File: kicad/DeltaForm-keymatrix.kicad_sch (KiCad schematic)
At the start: 45 parts

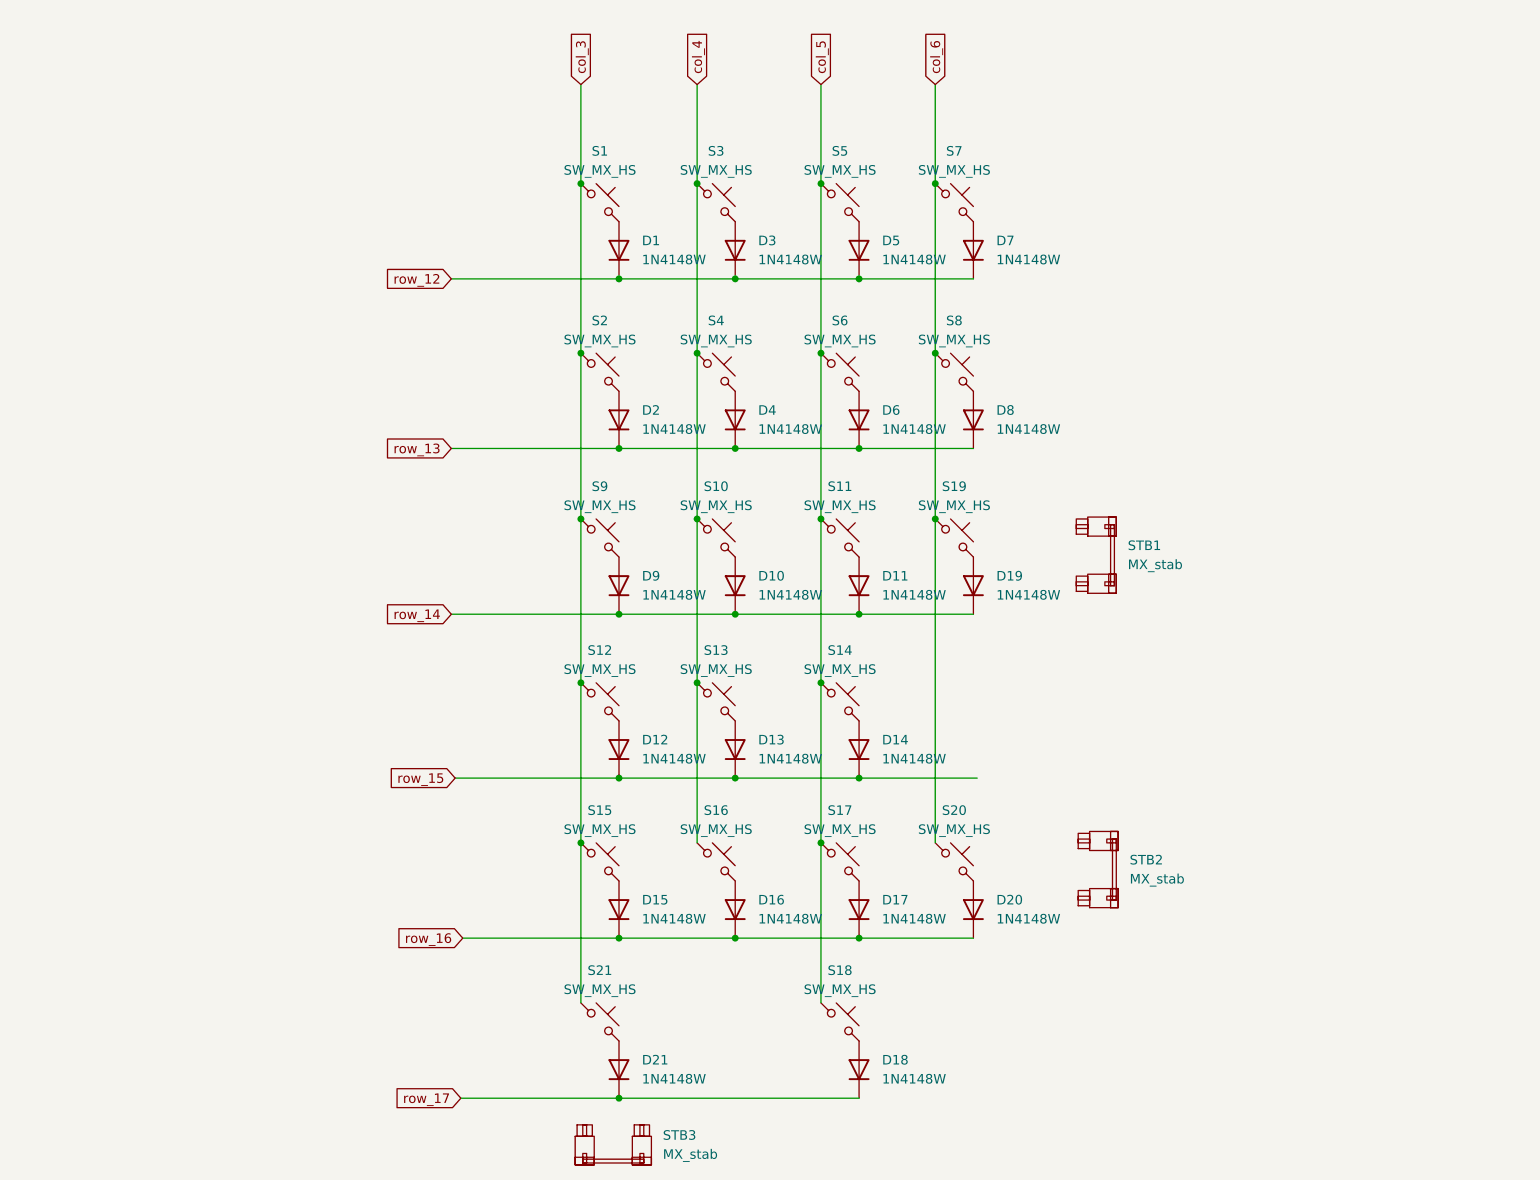
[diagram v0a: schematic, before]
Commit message: added MCU
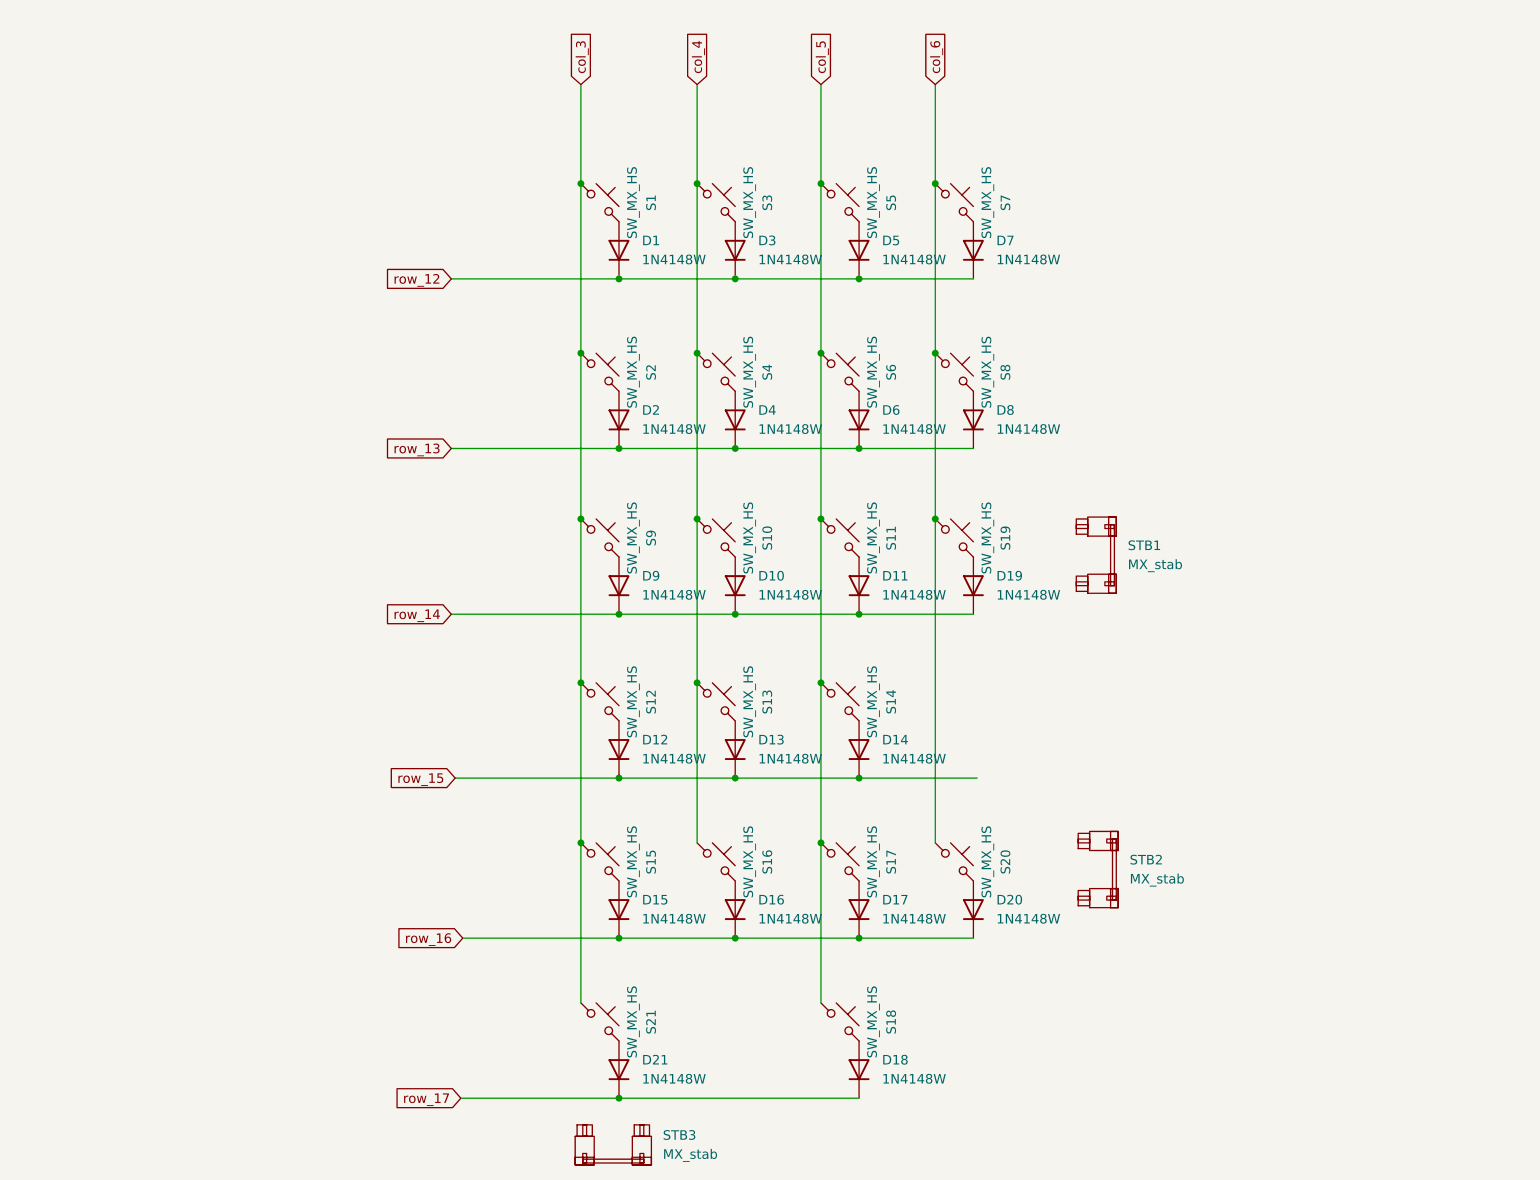
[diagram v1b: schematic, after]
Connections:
- net col_3: now also S1.2, S12.2, S15.2, S2.2, S21.2, S9.2; no longer S1.1, S12.1, S15.1, S2.1, S21.1, S9.1
- net col_4: now also S10.2, S13.2, S16.2, S3.2, S4.2; no longer S10.1, S13.1, S16.1, S3.1, S4.1
- net col_5: now also S11.2, S14.2, S17.2, S18.2, S5.2, S6.2; no longer S11.1, S14.1, S17.1, S18.1, S5.1, S6.1
- net col_6: now also S19.2, S20.2, S7.2, S8.2; no longer S19.1, S20.1, S7.1, S8.1
- net at D18.2 (A): now also S18.1; no longer S18.2
- net at D2.2 (A): now also S2.1; no longer S2.2
- net at D12.2 (A): now also S12.1; no longer S12.2
- net at D13.2 (A): now also S13.1; no longer S13.2
- net at D14.2 (A): now also S14.1; no longer S14.2
- net at D1.2 (A): now also S1.1; no longer S1.2
- net at D6.2 (A): now also S6.1; no longer S6.2
- net at D20.2 (A): now also S20.1; no longer S20.2
- net at D19.2 (A): now also S19.1; no longer S19.2
- net at D7.2 (A): now also S7.1; no longer S7.2
- net at D21.2 (A): now also S21.1; no longer S21.2
- net at D3.2 (A): now also S3.1; no longer S3.2
- net at D15.2 (A): now also S15.1; no longer S15.2
- net at D11.2 (A): now also S11.1; no longer S11.2
- net at D10.2 (A): now also S10.1; no longer S10.2
- net at D17.2 (A): now also S17.1; no longer S17.2
- net at D8.2 (A): now also S8.1; no longer S8.2
- net at D16.2 (A): now also S16.1; no longer S16.2
- net at D9.2 (A): now also S9.1; no longer S9.2
- net at D5.2 (A): now also S5.1; no longer S5.2
- net at D4.2 (A): now also S4.1; no longer S4.2
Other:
- moved on the sheet: S1, S10, S11, S12, S13, S14, S15, S16, S17, S18, S19, S2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

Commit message: pogo pin connectors
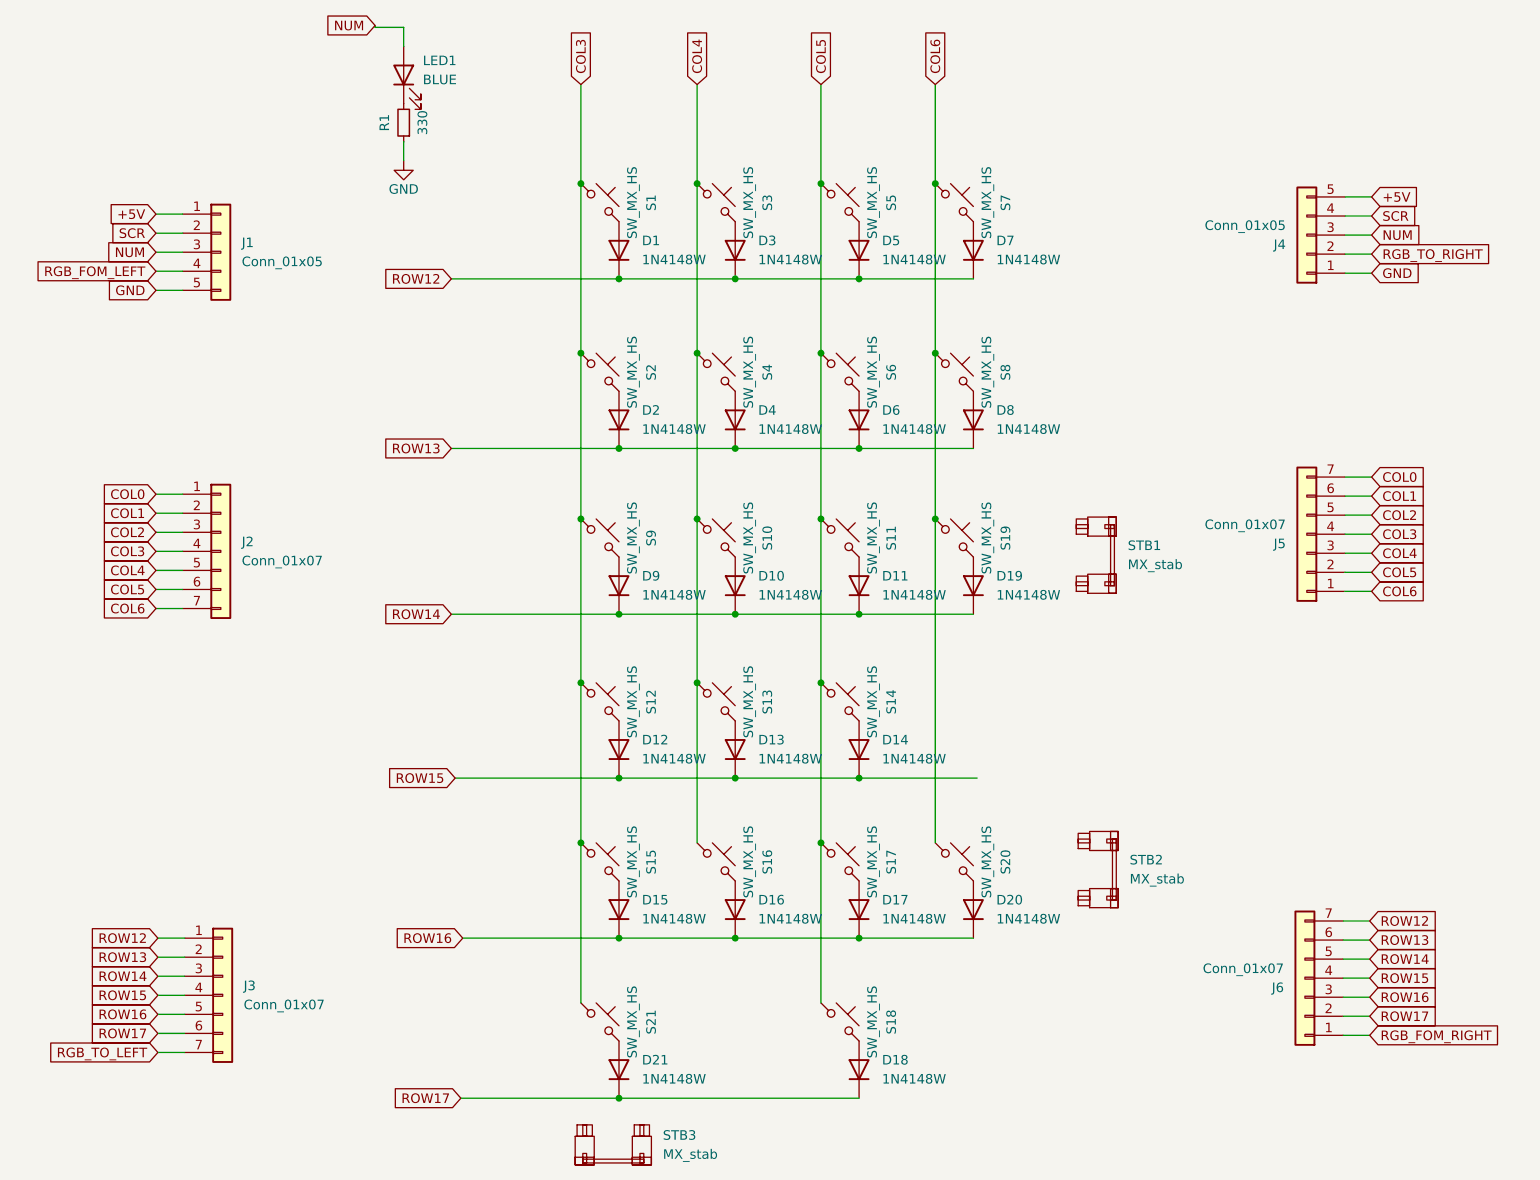
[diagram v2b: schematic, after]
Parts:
- added J1, J4: Conn_01x05, TB2086_MISC:Pogopin_1x05_P2.54mm_Curved, symbol Connector_Generic:Conn_01x05
- added J2, J3, J5, J6: Conn_01x07, symbol Connector_Generic:Conn_01x07
- added LED1: BLUE, LED_SMD:LED_0603_1608Metric_Pad1.05x0.95mm_HandSolder, symbol Device:LED
- added R1: 330, Resistor_SMD:R_0603_1608Metric, symbol Device:R_Small
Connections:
- net col_3 renamed COL3
- net COL3: now also J2.4 (Pin_4), J5.4 (Pin_4)
- net col_4 renamed COL4
- net COL4: now also J2.5 (Pin_5), J5.3 (Pin_3)
- net col_5 renamed COL5
- net COL5: now also J2.6 (Pin_6), J5.2 (Pin_2)
- net col_6 renamed COL6
- net COL6: now also J2.7 (Pin_7), J5.1 (Pin_1)
- net row_12 renamed ROW12
- net ROW12: now also J3.1 (Pin_1), J6.7 (Pin_7)
- net row_13 renamed ROW13
- net ROW13: now also J3.2 (Pin_2), J6.6 (Pin_6)
- net row_14 renamed ROW14
- net ROW14: now also J3.3 (Pin_3), J6.5 (Pin_5)
- net row_15 renamed ROW15
- net ROW15: now also J3.4 (Pin_4), J6.4 (Pin_4)
- net row_16 renamed ROW16
- net ROW16: now also J3.5 (Pin_5), J6.3 (Pin_3)
- net row_17 renamed ROW17
- net ROW17: now also J3.6 (Pin_6), J6.2 (Pin_2)
- new net: LED1.1 (K), R1.2
- new net +5V: J1.1 (Pin_1), J4.5 (Pin_5)
- new net COL0: J2.1 (Pin_1), J5.7 (Pin_7)
- new net COL1: J2.2 (Pin_2), J5.6 (Pin_6)
- new net COL2: J2.3 (Pin_3), J5.5 (Pin_5)
- new net GND: J1.5 (Pin_5), J4.1 (Pin_1), R1.1
- new net NUM: J1.3 (Pin_3), J4.3 (Pin_3), LED1.2 (A)
- new net RGB_FOM_LEFT: J1.4 (Pin_4)
- new net RGB_FOM_RIGHT: J6.1 (Pin_1)
- new net RGB_TO_LEFT: J3.7 (Pin_7)
- new net RGB_TO_RIGHT: J4.2 (Pin_2)
- new net SCR: J1.2 (Pin_2), J4.4 (Pin_4)

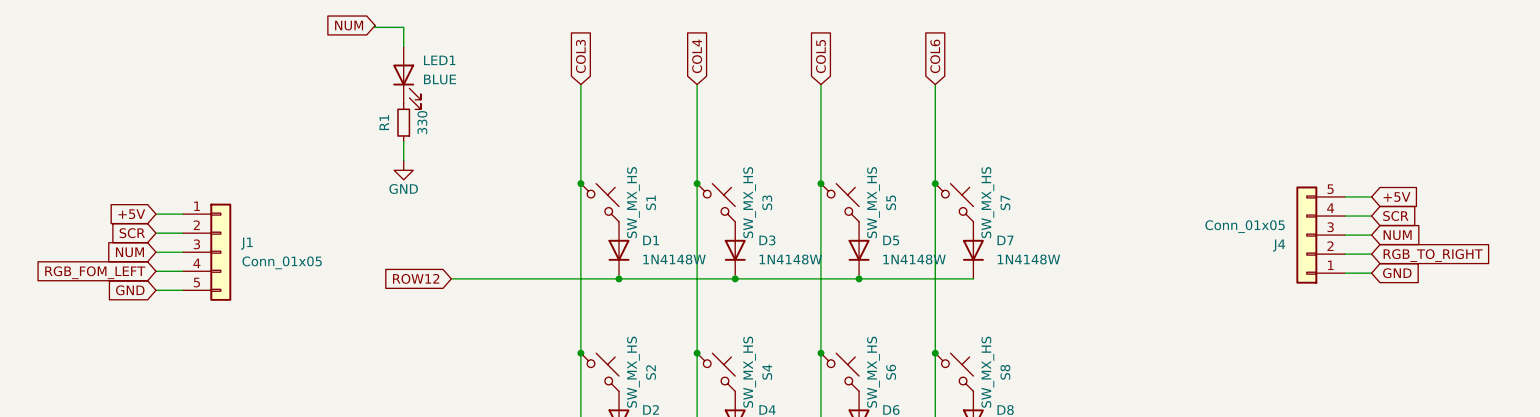
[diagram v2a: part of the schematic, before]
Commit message: screw holes
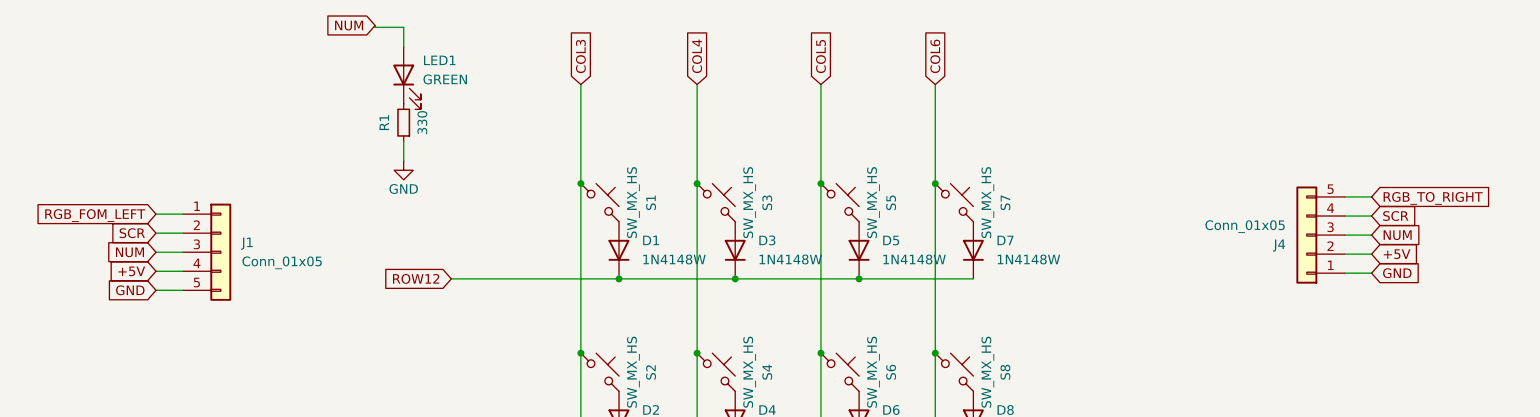
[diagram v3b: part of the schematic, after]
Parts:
- J2, J3, J5, J6: footprint (none) -> TB2086_MISC:Pogopin_1x07_P2.54mm_Curved
- LED1: value BLUE -> GREEN
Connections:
- net +5V: now also J1.4 (Pin_4), J4.2 (Pin_2); no longer J1.1 (Pin_1), J4.5 (Pin_5)
- net RGB_FOM_LEFT: now also J1.1 (Pin_1); no longer J1.4 (Pin_4)
- net RGB_TO_RIGHT: now also J4.5 (Pin_5); no longer J4.2 (Pin_2)
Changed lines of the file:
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@@
 		)
 	)
-	(global_label "RGB_FOM_LEFT"
+	(global_label "+5V"
 		(shape input)
 		(at 42.672 53.34 180)
@@
 		)
 		(property "Intersheetrefs" "${INTERSHEET_REFS}"
-			(at 25.8378 53.34 0)
+			(at 35.8163 53.34 0)
 			(effects
 				(font
@@
 		)
 	)
-	(global_label "RGB_TO_RIGHT"
+	(global_label "+5V"
 		(shape input)
 		(at 204.724 51.054 0)
@@
 		)
 		(property "Intersheetrefs" "${INTERSHEET_REFS}"
-			(at 221.1954 51.054 0)
+			(at 211.5797 51.054 0)
 			(effects
 				(font
@@
 		)
 	)
-	(global_label "+5V"
+	(global_label "RGB_FOM_LEFT"
 		(shape input)
 		(at 42.672 45.72 180)
@@
 		)
 		(property "Intersheetrefs" "${INTERSHEET_REFS}"
-			(at 35.8163 45.72 0)
+			(at 25.8378 45.72 0)
 			(effects
 				(font
@@
 		)
 	)
-	(global_label "+5V"
+	(global_label "RGB_TO_RIGHT"
 		(shape input)
 		(at 204.724 43.434 0)
@@
 		)
 		(property "Intersheetrefs" "${INTERSHEET_REFS}"
-			(at 211.5797 43.434 0)
+			(at 221.1954 43.434 0)
 			(effects
 				(font
@@
 			)
 		)
-		(property "Footprint" ""
+		(property "Footprint" "TB2086_MISC:Pogopin_1x07_P2.54mm_Curved"
 			(at 51.308 90.678 0)
 			(effects
@@
 			)
 		)
-		(property "Footprint" ""
+		(property "Footprint" "TB2086_MISC:Pogopin_1x07_P2.54mm_Curved"
 			(at 51.562 149.86 0)
 			(effects
@@
 			)
 		)
-		(property "Footprint" ""
+		(property "Footprint" "TB2086_MISC:Pogopin_1x07_P2.54mm_Curved"
 			(at 195.834 147.574 0)
 			(effects
@@
 			)
 		)
-		(property "Footprint" ""
+		(property "Footprint" "TB2086_MISC:Pogopin_1x07_P2.54mm_Curved"
 			(at 196.088 88.392 0)
 			(effects
@@
 			)
 		)
-		(property "Value" "BLUE"
+		(property "Value" "GREEN"
 			(at 78.232 27.813 90)
 			(effects

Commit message: artwork for DeltaForm
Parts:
- renumbered J1 to POGO1, J4 to POGO2, J2 to POGO3, J5 to POGO4, J3 to POGO5, J6 to POGO6
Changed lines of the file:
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@@
 		(dnp no)
 		(fields_autoplaced yes)
-		(property "Reference" "J1"
+		(property "Reference" "POGO1"
 			(at 54.102 49.5299 0)
 			(effects
@@
 			(project "DeltaForm"
 				(path "/c7177d09-71a2-4de7-9a3e-bfc16a7f2797/07d799b8-8bd0-4b35-b9da-910e8fb4f070"
-					(reference "J1")
+					(reference "POGO1")
 					(unit 1)
 				)
@@
 		(dnp no)
 		(fields_autoplaced yes)
-		(property "Reference" "J2"
+		(property "Reference" "POGO3"
 			(at 54.102 89.4079 0)
 			(effects
@@
 			(project "DeltaForm"
 				(path "/c7177d09-71a2-4de7-9a3e-bfc16a7f2797/07d799b8-8bd0-4b35-b9da-910e8fb4f070"
-					(reference "J2")
+					(reference "POGO3")
 					(unit 1)
 				)
@@
 		(dnp no)
 		(fields_autoplaced yes)
-		(property "Reference" "J3"
+		(property "Reference" "POGO5"
 			(at 54.356 148.5899 0)
 			(effects
@@
 			(project "DeltaForm"
 				(path "/c7177d09-71a2-4de7-9a3e-bfc16a7f2797/07d799b8-8bd0-4b35-b9da-910e8fb4f070"
-					(reference "J3")
+					(reference "POGO5")
 					(unit 1)
 				)
@@
 		(on_board yes)
 		(dnp no)
-		(property "Reference" "J6"
+		(property "Reference" "POGO6"
 			(at 193.04 148.8441 0)
 			(effects
@@
 			(project "DeltaForm"
 				(path "/c7177d09-71a2-4de7-9a3e-bfc16a7f2797/07d799b8-8bd0-4b35-b9da-910e8fb4f070"
-					(reference "J6")
+					(reference "POGO6")
 					(unit 1)
 				)
@@
 		(on_board yes)
 		(dnp no)
-		(property "Reference" "J5"
+		(property "Reference" "POGO4"
 			(at 193.294 89.6621 0)
 			(effects
@@
 			(project "DeltaForm"
 				(path "/c7177d09-71a2-4de7-9a3e-bfc16a7f2797/07d799b8-8bd0-4b35-b9da-910e8fb4f070"
-					(reference "J5")
+					(reference "POGO4")
 					(unit 1)
 				)
@@
 		(on_board yes)
 		(dnp no)
-		(property "Reference" "J4"
+		(property "Reference" "POGO2"
 			(at 193.294 49.7841 0)
 			(effects
@@
 			(project "DeltaForm"
 				(path "/c7177d09-71a2-4de7-9a3e-bfc16a7f2797/07d799b8-8bd0-4b35-b9da-910e8fb4f070"
-					(reference "J4")
-					(unit 1)
-				)
+					(reference "POGO2")
+					(unit 1)
+				)
